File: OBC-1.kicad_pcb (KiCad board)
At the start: 6 copper layers, 42.8 x 42.8 mm, 110 parts, among them J1 ERM8-020-X, J2 ERF6-020-X, J3 Conn_01x02_Female, Q1 MGSF1N02L, Q2 MGSF1N02L, U11 TMS5701227CZWTQQ1, U3 LTC4353, U4 SN65HVD230M-EP, U5 SN65HVD230M-EP, U6 SN65HVD230M-EP

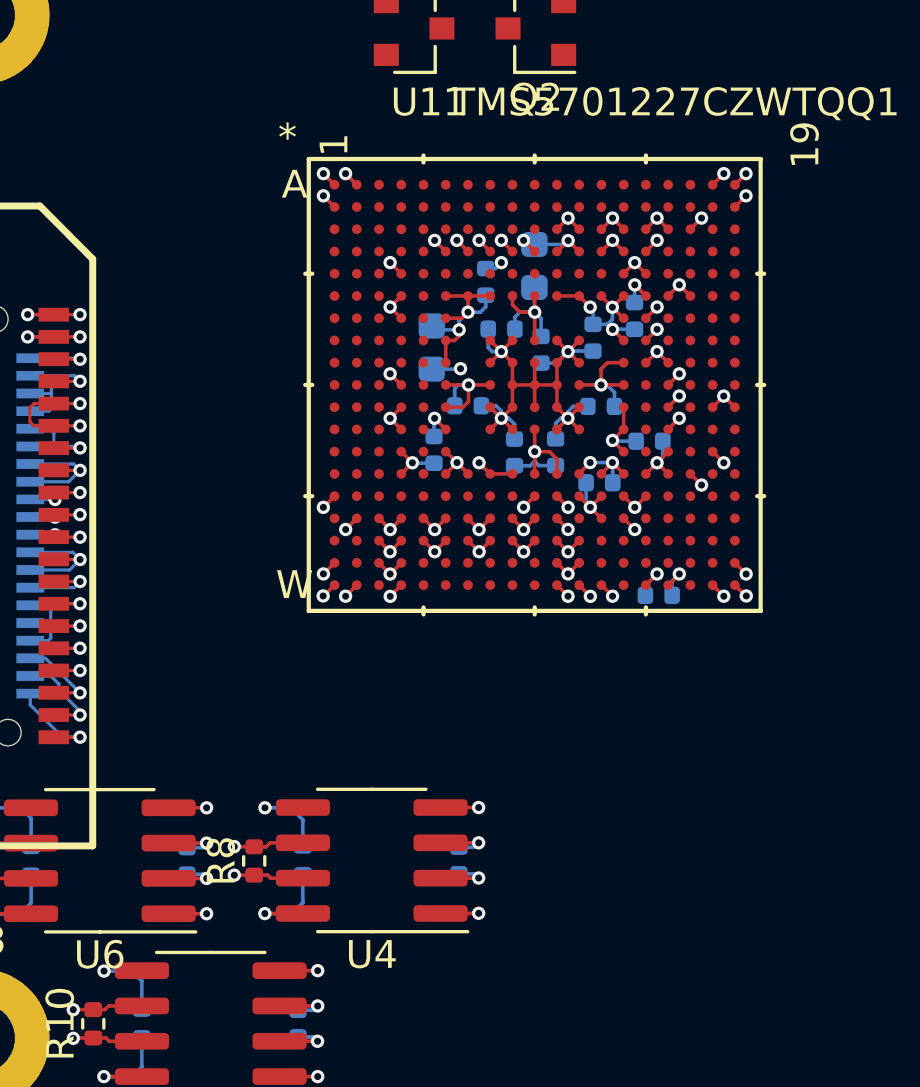
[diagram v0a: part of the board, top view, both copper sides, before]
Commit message: signals broken out from TMS570
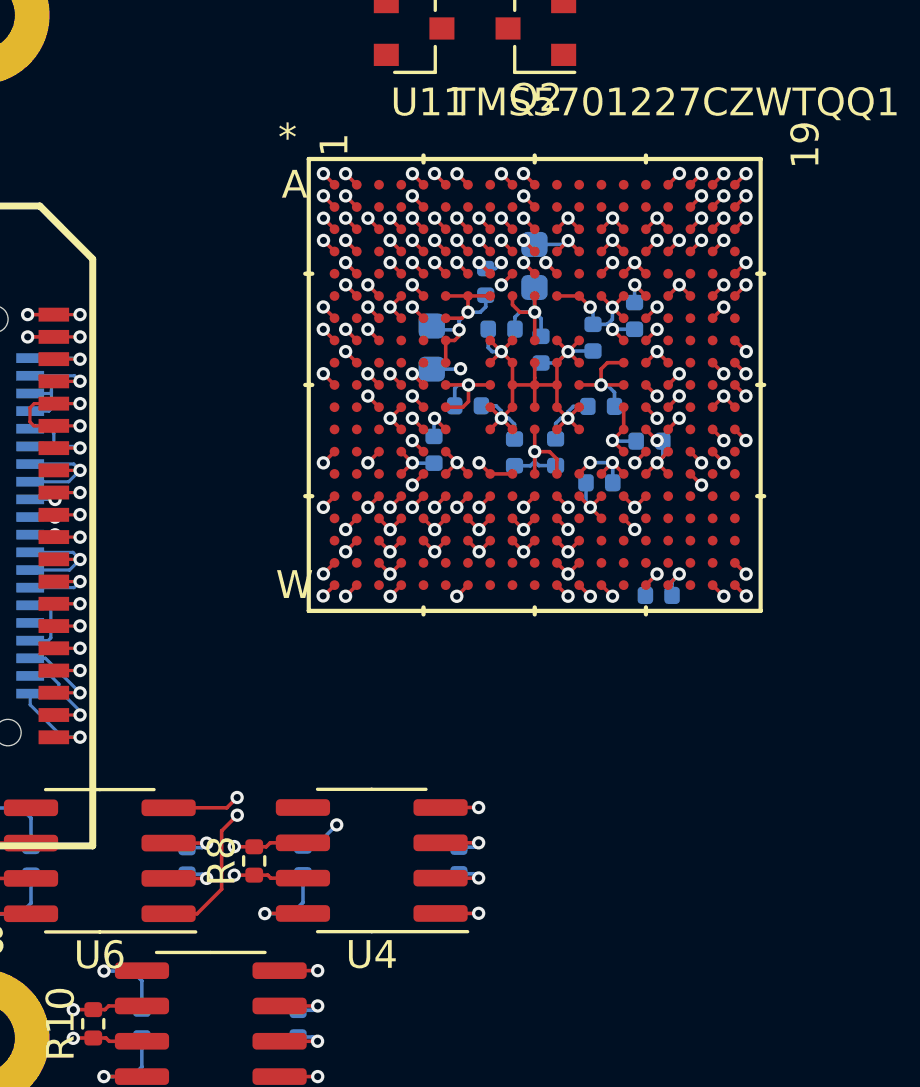
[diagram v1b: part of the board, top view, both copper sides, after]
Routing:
- net /TMS570_uC/CAN_PA_D: track 1.37 -> 5.74 mm, vias 1 -> 2
- net /TMS570_uC/CAN_PA_R: track 1.37 -> 3.18 mm, vias 1 -> 2
- net /Supervisor_RTC_FRAM/SPVSR_CLK: track 0.00 -> 0.57 mm, vias 0 -> 1
- net /TMS570_uC/JTAG_RTCK: track 0.00 -> 0.57 mm, vias 0 -> 1
- net /Connectors/GPS_P1PPS: track 0.94 -> 1.51 mm, vias 1 -> 2
- net /CAN_XCVR_R/CAN_PL_R: track 1.37 -> 1.94 mm, vias 1 -> 2
- net /CAN_XCVR_R/CAN_PL_Rs: track 2.53 -> 3.10 mm, vias 1 -> 2
- net /CAN_XCVR_PL/CAN_PL_D: track 1.37 -> 1.94 mm, vias 1 -> 2
- net /TMS570_uC/uC_OSC_IN: track 0.00 -> 0.57 mm, vias 0 -> 1
- net /Supervisor_RTC_FRAM/SPVSR_nRST: track 0.00 -> 0.57 mm, vias 0 -> 1
- net /Supervisor_RTC_FRAM/SPVSR_ACS: track 0.00 -> 0.57 mm, vias 0 -> 1
- net /TMS570_uC/DQ7: track 0.00 -> 0.57 mm, vias 0 -> 1
- net /TMS570_uC/A4: track 0.00 -> 0.57 mm, vias 0 -> 1
- net /TMS570_uC/DQ12: track 0.00 -> 0.57 mm, vias 0 -> 1
- net /TMS570_uC/A1: track 0.00 -> 0.57 mm, vias 0 -> 1
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
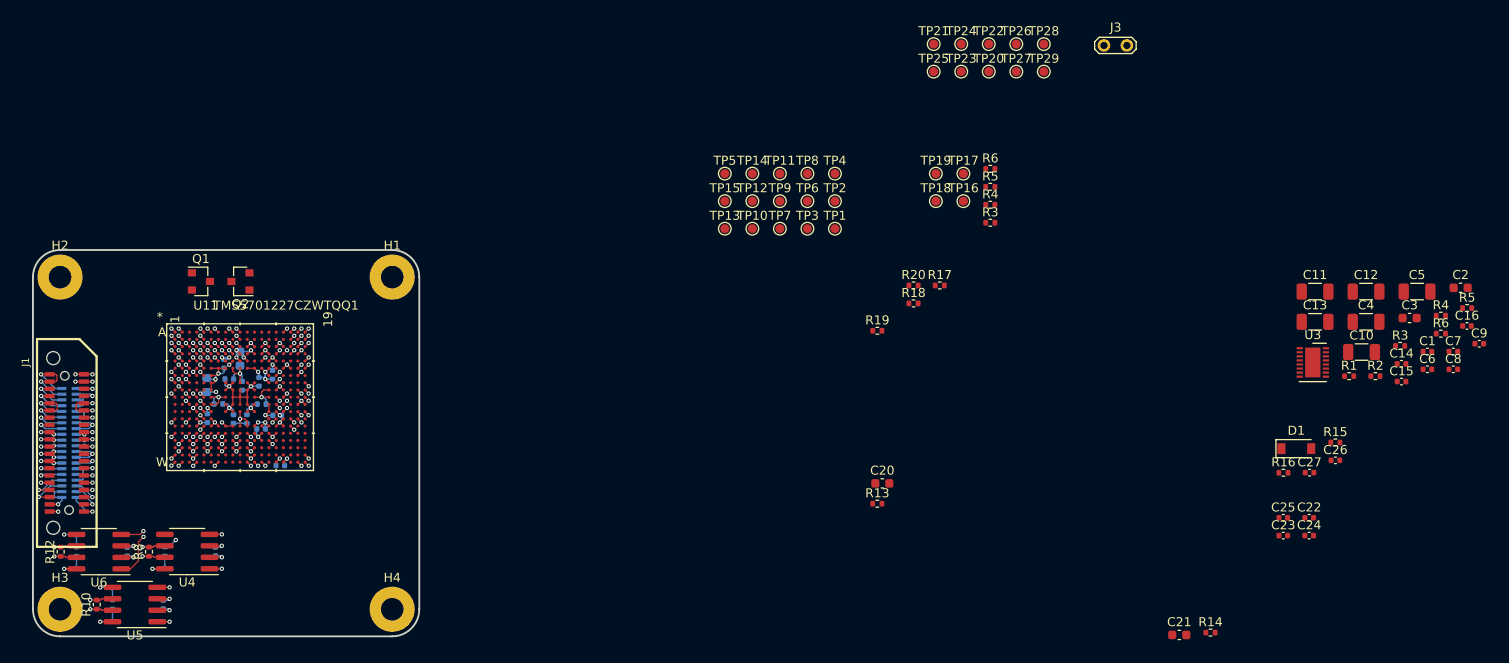
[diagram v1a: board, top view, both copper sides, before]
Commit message: added board level bulk decoupling
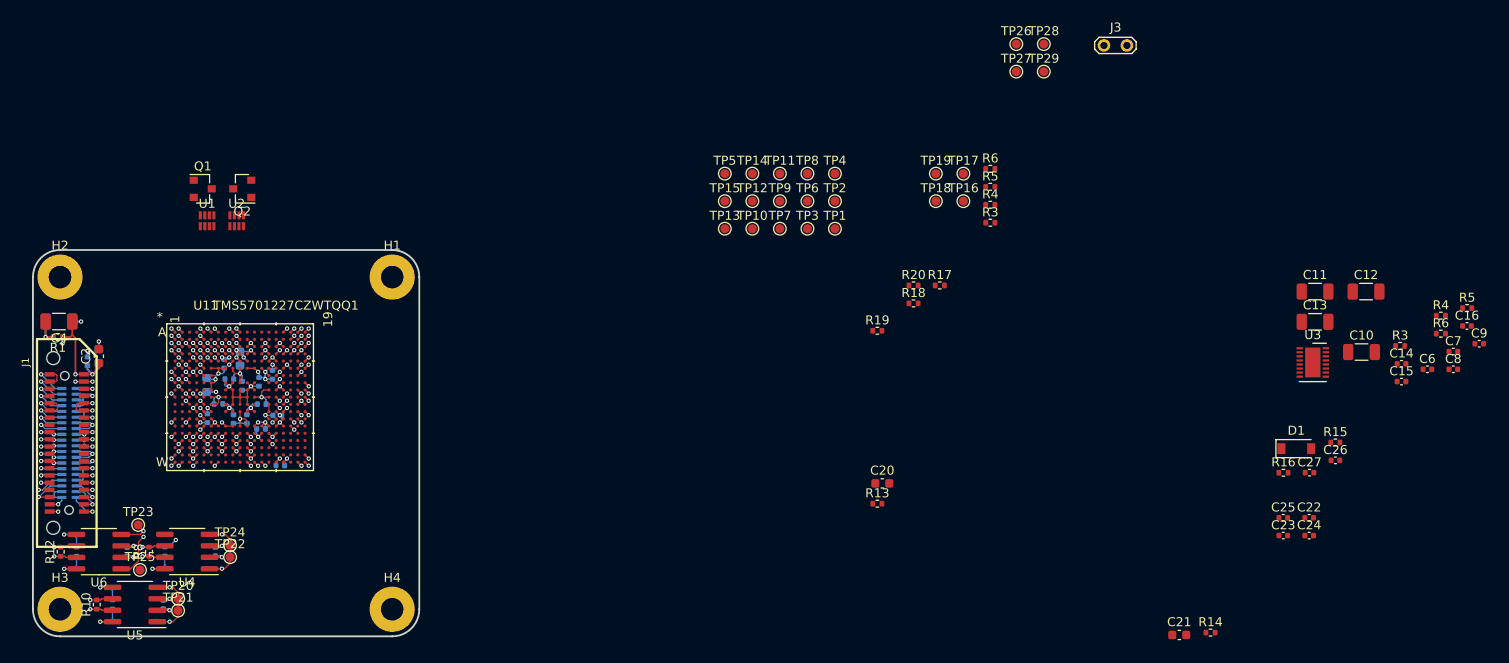
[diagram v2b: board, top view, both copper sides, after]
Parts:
- added U1: TPS62850x-Q1, TFT_SOT:SOT-583, F.Cu at (107.4, 68.9)
- added U2: TPS62850x-Q1, TFT_SOT:SOT-583, F.Cu at (110.7, 68.9)
- C1, C3, C5, R2: moved to B.Cu
- moved C2 151.1 mm to (96.2, 83.3), turned to 90 degrees
- moved C5 150.5 mm to (91.8, 79.4)
- moved C1 148.5 mm to (94.9, 83.8), turned to 90 degrees
- moved R2 146.0 mm to (91.7, 81.1)
- moved C3 145.3 mm to (96.2, 83.3), turned to 90 degrees
- moved C4 144.8 mm to (91.8, 79.4), turned to 180 degrees
- moved R1 143.1 mm to (91.7, 81.1), turned to 180 degrees
- moved TP20 107.1 mm to (105.0, 110.1)
- moved TP21 104.6 mm to (105.0, 111.4)
- moved TP23 104.1 mm to (100.6, 102.0)
- moved TP25 103.8 mm to (100.8, 106.9)
- moved TP22 101.5 mm to (110.7, 105.5)
- moved TP24 98.2 mm to (110.7, 104.2)
- moved Q1 10.3 mm to (107.7, 64.7)
- moved Q2 10.3 mm to (112.1, 64.7)
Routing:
- net OBC_3V3: track 40.9 -> 52.3 mm
- net Net-(C4-Pad2): track 0.00 -> 5.16 mm, vias 0 -> 1
- net GND: track 159.3 -> 163.4 mm, vias 102 -> 106
- net /CAN_XCVR_R/CAN_PL_R: track 1.94 -> 3.81 mm
- net /CAN_XCVR_R/CAN_PL_D: track 1.94 -> 3.78 mm
- net /CAN_XCVR_PL/CAN_PL_D: track 1.94 -> 3.78 mm
- net /CAN_XCVR_PL/CAN_PL_R: track 1.93 -> 3.73 mm
- net /TMS570_uC/CAN_PA_R: track 3.18 -> 4.11 mm
- net /TMS570_uC/CAN_PA_D: track 5.74 -> 6.59 mm

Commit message: first power supply laid out
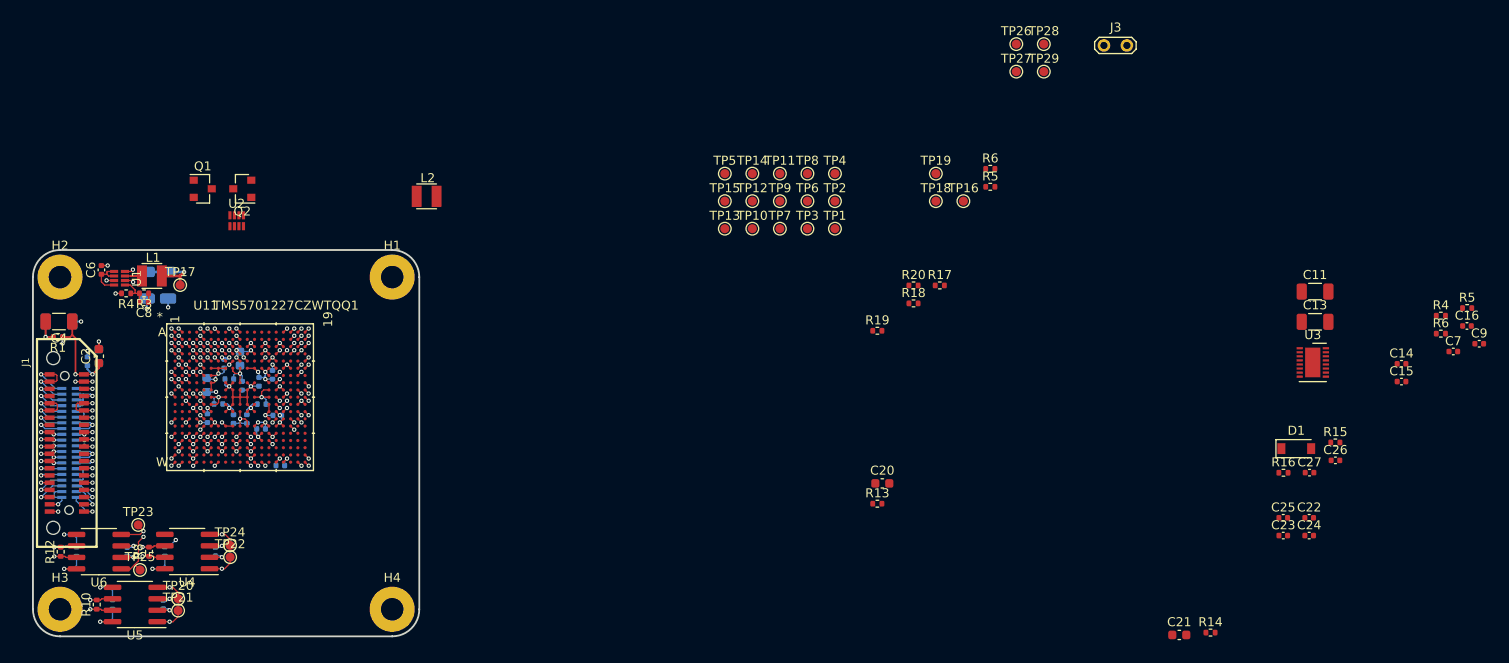
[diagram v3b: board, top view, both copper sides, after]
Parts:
- removed the R3 at (240.4, 82.1)
- added L1: 470nH-4A-20%, TFT_I_passive_SMD:2.5x2mm_I_SMD, F.Cu at (102.1, 74.4)
- added L2: 470nH-4A-20%, TFT_I_passive_SMD:2.5x2mm_I_SMD, F.Cu at (132.5, 65.6)
- C10, C12: moved to B.Cu
- moved C6 147.3 mm to (96.5, 73.7), turned to 90 degrees
- moved C8 145.2 mm to (101.2, 77.3), turned to 180 degrees
- moved C10 134.8 mm to (101.5, 75.4), turned to 270 degrees
- moved C12 132.7 mm to (103.9, 75.4), turned to 270 degrees
- moved R4 96.2 mm to (99.2, 76.3), turned to 180 degrees
- moved R3 94.1 mm to (101.2, 76.3), turned to 180 degrees
- moved TP17 87.6 mm to (105.2, 75.4)
- moved U1 10.8 mm to (97.9, 73.9), turned to 270 degrees
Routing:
- net OBC_1V25_P: track 0.00 -> 8.80 mm, vias 0 -> 1
- net GND: track 163.4 -> 169.6 mm, vias 106 -> 113
- net OBC_3V3: track 52.3 -> 57.3 mm
- net Net-(C8-Pad2): track 0.00 -> 3.69 mm
- net Net-(L1-Pad1): track 0.00 -> 1.89 mm
- net /Connectors/CAN_H_PA: track 14.1 -> 13.4 mm

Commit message: updated passive footprints, fixed errors, re-laid out CAN xcvrs
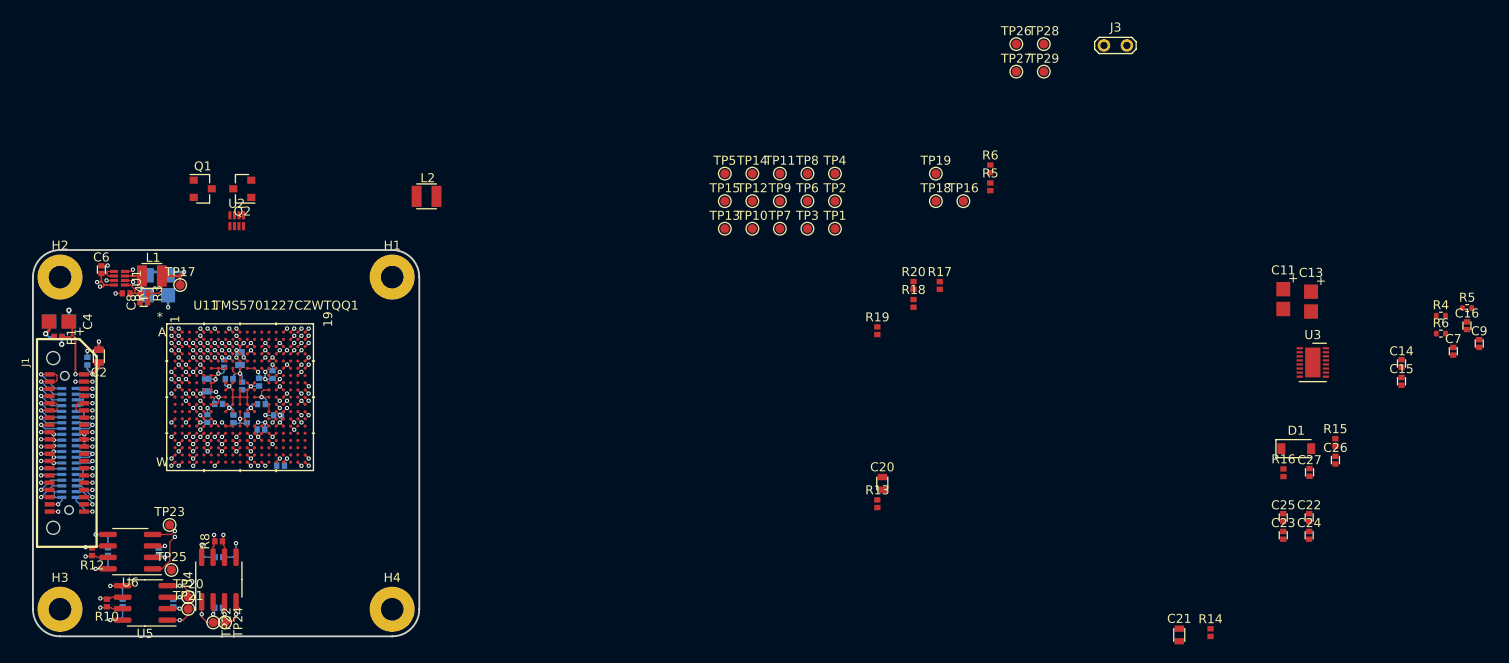
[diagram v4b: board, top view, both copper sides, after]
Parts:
- C1, C14, C15, C16, C17, C18, C19, C22, C23, C24, C25, C26, C27, C30, C31, C32, C33, C34, C35, C36, C37, C38, C39, C40, C41, C42, C6, C7, C8, C9: footprint Capacitor_SMD:C_0402_1005Metric -> TFT_C_passive_SMD:0402_CAP
- C10, C11, C12, C13, C4, C5: footprint Capacitor_SMD:C_1206_3216Metric -> TFT_C_passive_SMD:1206_CAP_TANT
- C2, C20, C21, C28, C29, C3: footprint Capacitor_SMD:C_0603_1608Metric -> TFT_C_passive_SMD:0603_CAP
- R1, R10, R11, R12, R13, R14, R15, R16, R17, R18, R19, R2, R20, R3, R4, R5, R6, R7, R8, R9: footprint Resistor_SMD:R_0402_1005Metric -> TFT_R_passive_SMD:0402_RES
- moved TP24 8.55 mm to (110.2, 112.8), turned to 270 degrees
- moved R8 7.80 mm to (109.5, 103.8)
- moved TP22 7.48 mm to (108.9, 112.8), turned to 270 degrees
- moved C17 6.24 mm to (109.5, 111.1)
- moved R7 6.02 mm to (109.5, 105.5), turned to 90 degrees
- moved U4 4.68 mm to (109.5, 108.0), turned to 90 degrees
- moved C11 3.61 mm to (227.4, 76.9)
- moved TP25 3.48 mm to (104.2, 106.9)
- moved U6 3.48 mm to (99.7, 104.9)
- moved C19 3.48 mm to (102.8, 104.9), turned to 0 degrees
- moved R11 3.48 mm to (97.2, 104.9), turned to 180 degrees
- moved R12 3.48 mm to (95.5, 104.9), turned to 180 degrees
- moved TP23 3.48 mm to (104.0, 102.0)
- moved C13 2.28 mm to (230.5, 77.2)
- moved R10 1.13 mm to (97.1, 110.6), turned to 180 degrees
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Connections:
- J1 pad 19: /CAN_XCVR_R/CAN_L_PL -> /CAN_XCVR_R/CAN_H_PL
- J1 pad 20: /CAN_XCVR_R/CAN_H_PL -> /CAN_XCVR_R/CAN_L_PL
- J2 pad 19: /CAN_XCVR_R/CAN_L_PL -> /CAN_XCVR_R/CAN_H_PL
- J2 pad 20: /CAN_XCVR_R/CAN_H_PL -> /CAN_XCVR_R/CAN_L_PL
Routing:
- net /CAN_XCVR_PL/CAN_L_PL: track 13.7 -> 20.9 mm
- net /CAN_XCVR_PL/CAN_H_PL: track 13.9 -> 19.3 mm
- net /Connectors/CAN_L_PA: track 13.5 -> 17.6 mm
- net /Connectors/CAN_H_PA: track 13.4 -> 16.9 mm
- net OBC_1V25_P: track 8.80 -> 12.0 mm
- net /CAN_XCVR_R/CAN_H_PL: track 17.6 -> 19.8 mm
- net GND: track 169.6 -> 168.1 mm, vias 113 -> 112
- net /CAN_XCVR_PL/CAN_PL_Rs: track 2.09 -> 3.27 mm
- net OBC_3V3: track 57.3 -> 58.4 mm, vias 19 -> 21
- net Net-(C4-Pad2): track 5.16 -> 4.11 mm
- net /CAN_XCVR_R/CAN_L_PL: track 17.3 -> 18.2 mm

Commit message: initial layout of 2nd power supply done, 3V3 plane routing to the supply inputs needs work, currently too broken up by ground vias
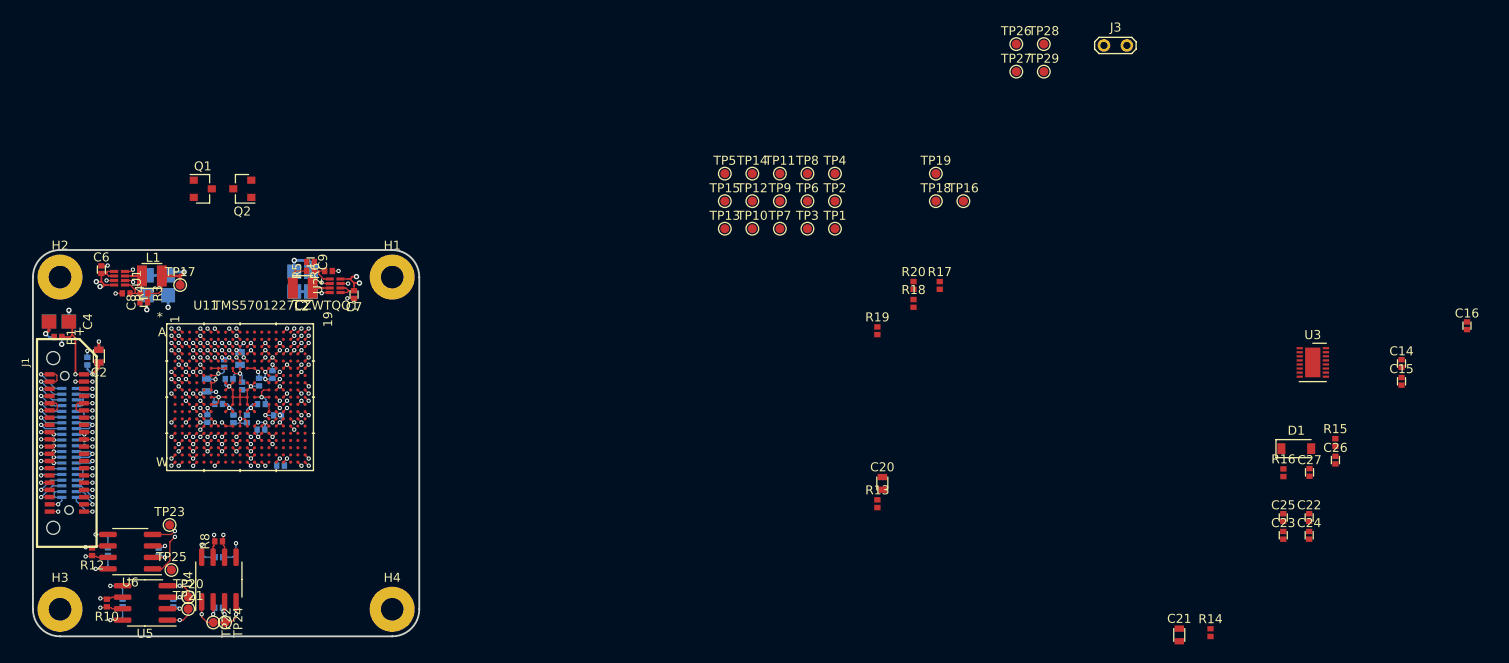
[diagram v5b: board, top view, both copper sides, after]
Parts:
- removed the R4 at (244.9, 78.8)
- removed the R5 at (247.8, 77.9)
- removed the R6 at (244.9, 80.8)
- C11, C13: moved to B.Cu
- moved C9 129.8 mm to (119.6, 72.8), turned to 270 degrees
- moved C7 121.9 mm to (124.5, 76.4), turned to 180 degrees
- moved C13 112.7 mm to (117.8, 75.0)
- moved C11 107.7 mm to (119.7, 75.0)
- moved R5 75.9 mm to (119.7, 73.8), turned to 90 degrees
- moved R6 74.2 mm to (121.6, 73.8), turned to 90 degrees
- moved L2 17.1 mm to (118.8, 75.7), turned to 180 degrees
- moved U2 14.3 mm to (123.0, 76.2), turned to 90 degrees
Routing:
- net GND: track 168.1 -> 178.0 mm, vias 112 -> 119
- net OBC_3V3: track 58.4 -> 65.1 mm, vias 21 -> 23
- net OBC_1V2_R: track 0.00 -> 6.13 mm
- net Net-(C9-Pad2): track 0.00 -> 3.91 mm
- net Net-(L2-Pad1): track 0.00 -> 1.89 mm
